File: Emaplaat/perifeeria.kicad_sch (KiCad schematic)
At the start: 28 parts, among them J3 Conn_01x05_Socket, Q1 2N7002K

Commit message: 2
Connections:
- net AGND is gone; now on net GND: C53.2, S5.3, S5.4
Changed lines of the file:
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@@
 			)
 		)
-		(property "Value" "AGND"
+		(property "Value" "GND"
 			(at 82.55 158.75 0)
 			(effects

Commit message: natuke parandusi
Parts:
- added D409: CPDH3V3UP-HF, Diode_SMD:D_SOD-523, symbol CPDH3V3UP-HF:CPDH3V3UP-HF
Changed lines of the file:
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@@
+	)
+	(symbol
+		(lib_name "CPDH3V3UP-HF_2")
+		(lib_id "CPDH3V3UP-HF:CPDH3V3UP-HF")
+		(at 57.15 165.1 270)
+		(unit 1)
+		(exclude_from_sim no)
+		(in_bom yes)
+		(on_board yes)
+		(dnp no)
+		(property "Reference" "D409"
+			(at 59.182 172.72 90)
+			(effects
+				(font
+					(size 1.27 1.27)
+				)
+				(justify left)
+			)
+		)
+		(property "Value" "CPDH3V3UP-HF"
+			(at 51.562 191.008 90)
+			(effects
+				(font
+					(size 1.27 1.27)
+				)
+				(justify left)
+			)
+		)
+		(property "Footprint" "Diode_SMD:D_SOD-523"
+			(at -36.5 175.26 0)
+			(effects
+				(font
+					(size 1.27 1.27)
+				)
+				(justify left bottom)
+				(hide yes)
+			)
+		)
+		(property "Datasheet" "https://datasheet.datasheetarchive.com/originals/distributors/Datasheets-DGA26/1842371.pdf"
+			(at -136.5 175.26 0)
+			(effects
+				(font
+					(size 1.27 1.27)
+				)
+				(justify left bottom)
+				(hide yes)
+			)
+		)
+		(property "Description" "ESD Suppressors / TVS Diodes 5.5V, 15Kv"
+			(at 70.866 164.846 0)
+			(effects
+				(font
+					(size 1.27 1.27)
+				)
+				(hide yes)
+			)
+		)
+		(property "Height" "0.77"
+			(at -336.5 175.26 0)
+			(effects
+				(font
+					(size 1.27 1.27)
+				)
+				(justify left bottom)
+				(hide yes)
+			)
+		)
+		(property "Mouser Part Number" "750-CPDH3V3UP-HF"
+			(at -436.5 175.26 0)
+			(effects
+				(font
+					(size 1.27 1.27)
+				)
+				(justify left bottom)
+				(hide yes)
+			)
+		)
+		(property "Mouser Price/Stock" "https://www.mouser.co.uk/ProductDetail/Comchip-Technology/CPDH3V3UP-HF?qs=XEIV%2Fho1H6em2DT135enQw%3D%3D"
+			(at -536.5 175.26 0)
+			(effects
+				(font
+					(size 1.27 1.27)
+				)
+				(justify left bottom)
+				(hide yes)
+			)
+		)
+		(property "Manufacturer_Name" "Comchip Technology"
+			(at -636.5 175.26 0)
+			(effects
+				(font
+					(size 1.27 1.27)
+				)
+				(justify left bottom)
+				(hide yes)
+			)
+		)
+		(property "Manufacturer_Part_Number" "CPDH3V3UP-HF"
+			(at -736.5 175.26 0)
+			(effects
+				(font
+					(size 1.27 1.27)
+				)
+				(justify left bottom)
+				(hide yes)
+			)
+		)
+		(property "Voltage" "3.3"
+			(at 65.278 192.786 90)
+			(effects
+				(font
+					(size 1.27 1.27)
+				)
+			)
+		)
+		(pin "2"
+		)
+		(pin "1"
+		)
+		(instances
+			(project "Emaplaat"
+				(path "/489224c0-ace1-4530-aa61-a5d03adf1434/ac5852bd-1625-445e-9b6b-b65a0daab019"
+					(reference "D409")
+					(unit 1)
+				)
+			)
+		)
 	)
 	(symbol

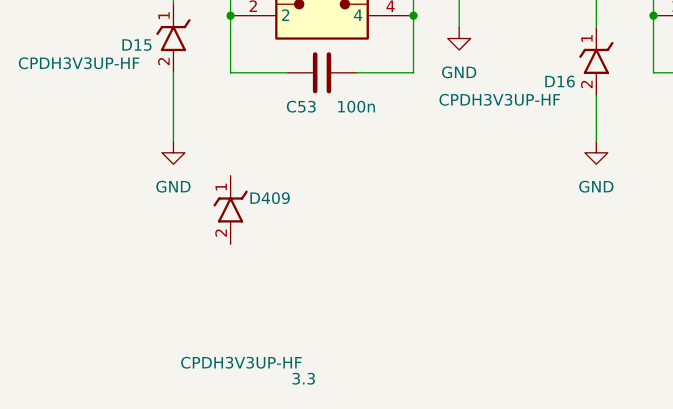
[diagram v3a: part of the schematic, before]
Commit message: Lisasin kondensaatorid, mis on >3.3u footprindi ja sümbolid. Sammuti liigutasin ESP32 ja USC-C ühendused plaadi äärtele
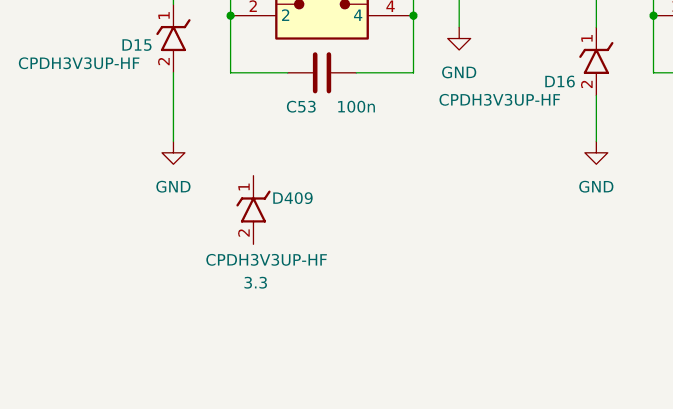
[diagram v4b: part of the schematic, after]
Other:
- moved on the sheet: D409
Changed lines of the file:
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@@
 		(lib_name "CPDH3V3UP-HF_2")
 		(lib_id "CPDH3V3UP-HF:CPDH3V3UP-HF")
-		(at 57.15 165.1 270)
+		(at 59.69 165.1 270)
 		(unit 1)
 		(exclude_from_sim no)
@@
 		(dnp no)
 		(property "Reference" "D409"
-			(at 59.182 172.72 90)
+			(at 61.722 172.72 90)
 			(effects
 				(font
@@
 		)
 		(property "Value" "CPDH3V3UP-HF"
-			(at 51.562 191.008 90)
+			(at 54.356 179.578 90)
 			(effects
 				(font
@@
 		)
 		(property "Footprint" "Diode_SMD:D_SOD-523"
-			(at -36.5 175.26 0)
+			(at -33.96 175.26 0)
 			(effects
 				(font
@@
 		)
 		(property "Datasheet" "https://datasheet.datasheetarchive.com/originals/distributors/Datasheets-DGA26/1842371.pdf"
-			(at -136.5 175.26 0)
+			(at -133.96 175.26 0)
 			(effects
 				(font
@@
 		)
 		(property "Description" "ESD Suppressors / TVS Diodes 5.5V, 15Kv"
-			(at 70.866 164.846 0)
+			(at 73.406 164.846 0)
 			(effects
 				(font
@@
 		)
 		(property "Height" "0.77"
-			(at -336.5 175.26 0)
+			(at -333.96 175.26 0)
 			(effects
 				(font
@@
 		)
 		(property "Mouser Part Number" "750-CPDH3V3UP-HF"
-			(at -436.5 175.26 0)
+			(at -433.96 175.26 0)
 			(effects
 				(font
@@
 		)
 		(property "Mouser Price/Stock" "https://www.mouser.co.uk/ProductDetail/Comchip-Technology/CPDH3V3UP-HF?qs=XEIV%2Fho1H6em2DT135enQw%3D%3D"
-			(at -536.5 175.26 0)
+			(at -533.96 175.26 0)
 			(effects
 				(font
@@
 		)
 		(property "Manufacturer_Name" "Comchip Technology"
-			(at -636.5 175.26 0)
+			(at -633.96 175.26 0)
 			(effects
 				(font
@@
 		)
 		(property "Manufacturer_Part_Number" "CPDH3V3UP-HF"
-			(at -736.5 175.26 0)
+			(at -733.96 175.26 0)
 			(effects
 				(font
@@
 		)
 		(property "Voltage" "3.3"
-			(at 65.278 192.786 90)
+			(at 59.944 182.118 90)
 			(effects
 				(font

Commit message: v1.1 kuid veel pooleli
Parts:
- removed D409: CPDH3V3UP-HF, Diode_SMD:D_SOD-523, symbol CPDH3V3UP-HF:CPDH3V3UP-HF
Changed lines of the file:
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@@
-	)
-	(symbol
-		(lib_name "CPDH3V3UP-HF_2")
-		(lib_id "CPDH3V3UP-HF:CPDH3V3UP-HF")
-		(at 59.69 165.1 270)
-		(unit 1)
-		(exclude_from_sim no)
-		(in_bom yes)
-		(on_board yes)
-		(dnp no)
-		(property "Reference" "D409"
-			(at 61.722 172.72 90)
-			(effects
-				(font
-					(size 1.27 1.27)
-				)
-				(justify left)
-			)
-		)
-		(property "Value" "CPDH3V3UP-HF"
-			(at 54.356 179.578 90)
-			(effects
-				(font
-					(size 1.27 1.27)
-				)
-				(justify left)
-			)
-		)
-		(property "Footprint" "Diode_SMD:D_SOD-523"
-			(at -33.96 175.26 0)
-			(effects
-				(font
-					(size 1.27 1.27)
-				)
-				(justify left bottom)
-				(hide yes)
-			)
-		)
-		(property "Datasheet" "https://datasheet.datasheetarchive.com/originals/distributors/Datasheets-DGA26/1842371.pdf"
-			(at -133.96 175.26 0)
-			(effects
-				(font
-					(size 1.27 1.27)
-				)
-				(justify left bottom)
-				(hide yes)
-			)
-		)
-		(property "Description" "ESD Suppressors / TVS Diodes 5.5V, 15Kv"
-			(at 73.406 164.846 0)
-			(effects
-				(font
-					(size 1.27 1.27)
-				)
-				(hide yes)
-			)
-		)
-		(property "Height" "0.77"
-			(at -333.96 175.26 0)
-			(effects
-				(font
-					(size 1.27 1.27)
-				)
-				(justify left bottom)
-				(hide yes)
-			)
-		)
-		(property "Mouser Part Number" "750-CPDH3V3UP-HF"
-			(at -433.96 175.26 0)
-			(effects
-				(font
-					(size 1.27 1.27)
-				)
-				(justify left bottom)
-				(hide yes)
-			)
-		)
-		(property "Mouser Price/Stock" "https://www.mouser.co.uk/ProductDetail/Comchip-Technology/CPDH3V3UP-HF?qs=XEIV%2Fho1H6em2DT135enQw%3D%3D"
-			(at -533.96 175.26 0)
-			(effects
-				(font
-					(size 1.27 1.27)
-				)
-				(justify left bottom)
-				(hide yes)
-			)
-		)
-		(property "Manufacturer_Name" "Comchip Technology"
-			(at -633.96 175.26 0)
-			(effects
-				(font
-					(size 1.27 1.27)
-				)
-				(justify left bottom)
-				(hide yes)
-			)
-		)
-		(property "Manufacturer_Part_Number" "CPDH3V3UP-HF"
-			(at -733.96 175.26 0)
-			(effects
-				(font
-					(size 1.27 1.27)
-				)
-				(justify left bottom)
-				(hide yes)
-			)
-		)
-		(property "Voltage" "3.3"
-			(at 59.944 182.118 90)
-			(effects
-				(font
-					(size 1.27 1.27)
-				)
-			)
-		)
-		(pin "2"
-		)
-		(pin "1"
-		)
-		(instances
-			(project "Emaplaat"
-				(path "/489224c0-ace1-4530-aa61-a5d03adf1434/ac5852bd-1625-445e-9b6b-b65a0daab019"
-					(reference "D409")
-					(unit 1)
-				)
-			)
-		)
 	)
 	(symbol
